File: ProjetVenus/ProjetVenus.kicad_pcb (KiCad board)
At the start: 2 copper layers, 41 parts, among them J1 Conn_01x02_Pin, J2 Conn_01x04_Pin, J4 Conn_01x02_Pin, J5 Conn_01x05_Pin, U1 ATtiny412-SS, U2 ADP2108AUJZ-3.0-R7, U3 MS5607-02BA

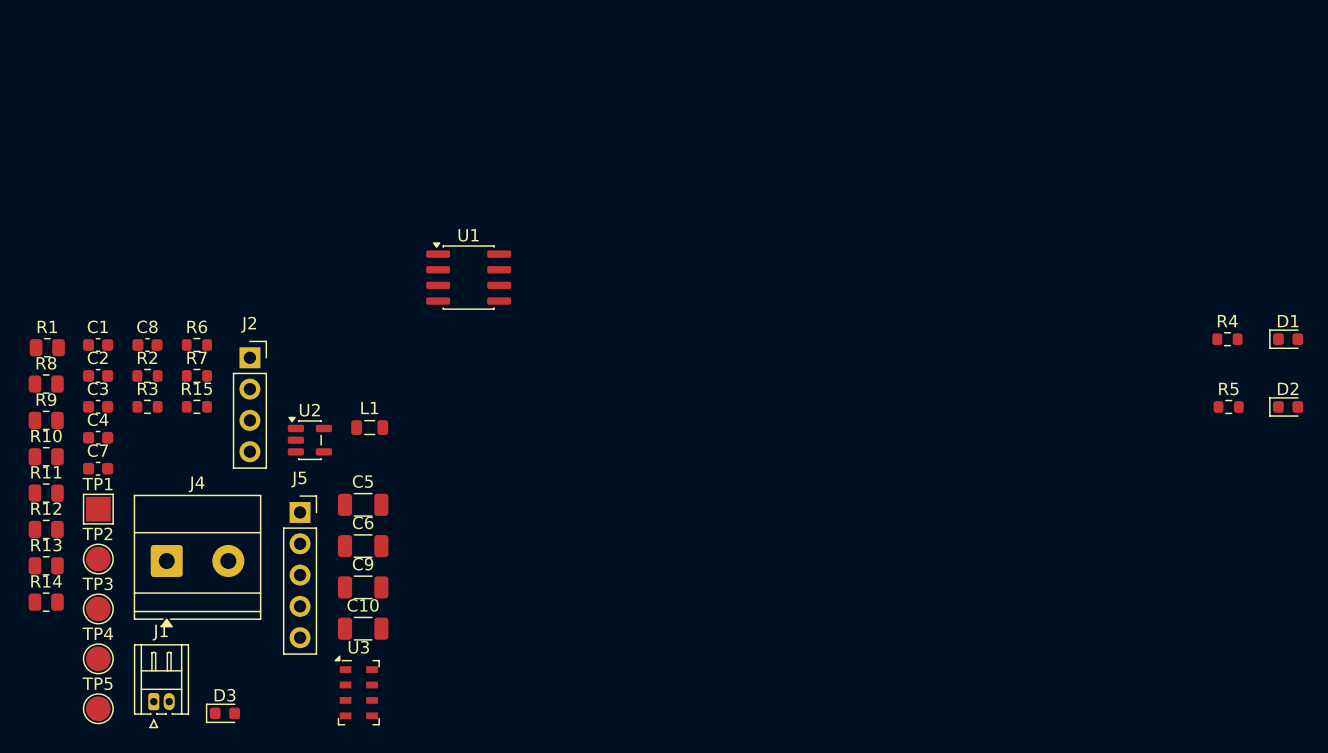
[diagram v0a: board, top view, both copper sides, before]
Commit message: V1.0
La chip U3 a du cosmétiques qui va disparaitre a moins qu'on change le footprint, mais on s'en fou un peu
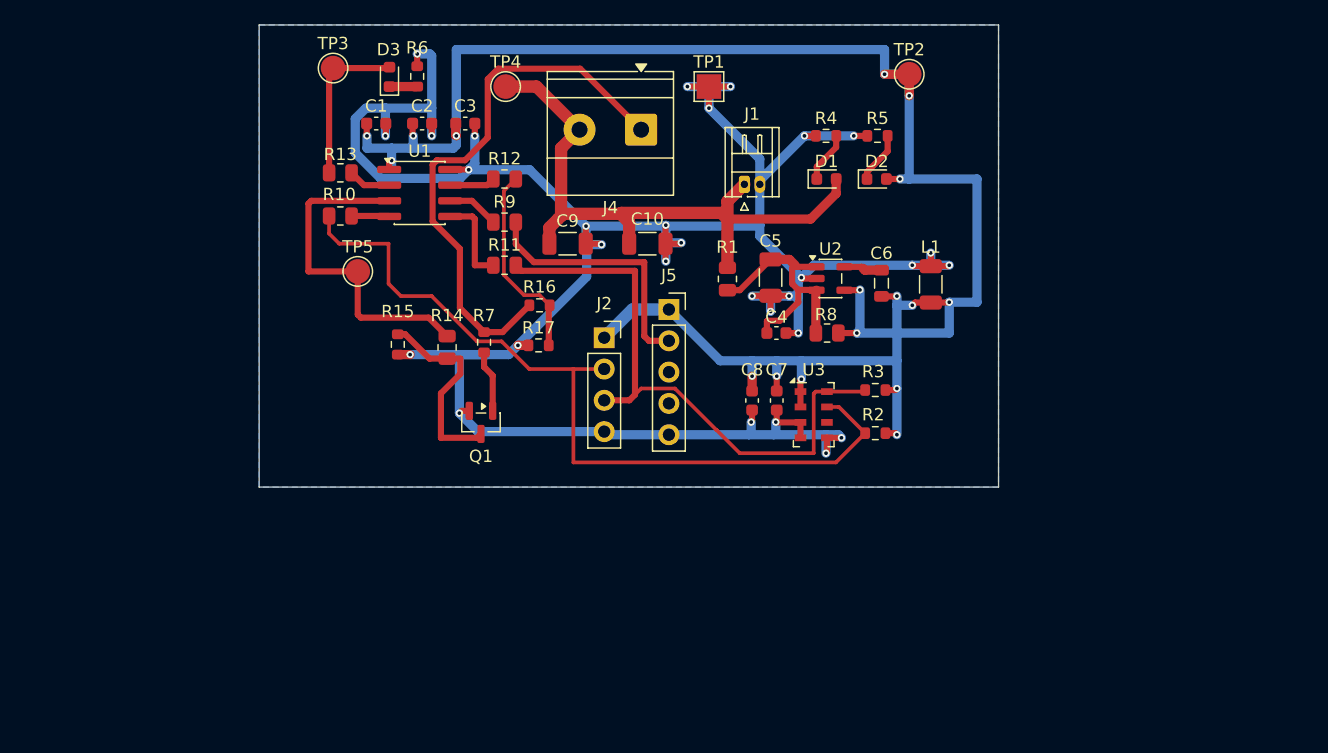
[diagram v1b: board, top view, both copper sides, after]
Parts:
- added Q1: Q_NMOS_GSD, Package_TO_SOT_SMD:SOT-23, F.Cu at (208.0, 122.2)
- added R16: 100k, Resistor_SMD:R_0603_1608Metric, F.Cu at (212.8, 112.8)
- added R17: 100k, Resistor_SMD:R_0603_1608Metric, F.Cu at (212.7, 116.0)
- R14: value TBD -> 220
- moved TP2 76.7 mm to (242.8, 94.0)
- moved J1 63.7 mm to (229.4, 102.9)
- moved R8 63.5 mm to (236.1, 115.0)
- moved TP1 60.3 mm to (226.5, 95.0)
- moved R2 59.2 mm to (240.0, 123.1)
- moved R3 59.1 mm to (240.0, 119.6)
- moved TP4 57.0 mm to (210.0, 95.0)
- moved C4 55.7 mm to (232.0, 115.0)
- moved R1 55.5 mm to (228.0, 110.6), turned to -90 degrees
- moved C7 55.3 mm to (232.0, 120.5), turned to -90 degrees
- moved D3 53.3 mm to (200.6, 94.2), turned to 90 degrees
- moved J4 52.0 mm to (221.0, 98.5), turned to 180 degrees
- moved C6 50.7 mm to (244.5, 111.0), turned to 90 degrees
- moved C8 49.3 mm to (230.0, 120.5), turned to -90 degrees
- moved TP3 47.8 mm to (196.0, 93.5)
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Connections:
- R12 pad 2: unconnected-(R12-Pad2) -> /EMATCH_DET
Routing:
- net GND: track 0.00 -> 222.7 mm, vias 0 -> 30
- net +3V0: track 0.00 -> 164.0 mm, vias 0 -> 17
- net /SDA: track 0.00 -> 66.4 mm
- net +BATT: track 0.00 -> 52.4 mm
- net /SCL: track 0.00 -> 49.1 mm
- net Net-(J4-Pin_1): track 0.00 -> 44.9 mm
- net /EMATCH: track 0.00 -> 27.6 mm
- net Net-(U2-EN): track 0.00 -> 21.1 mm
- net /UPDI: track 0.00 -> 21.0 mm
- net Net-(Q1-G): track 0.00 -> 16.7 mm
- net /EMATCH_DET: track 0.00 -> 16.2 mm
- net /LED: track 0.00 -> 13.2 mm
- net Net-(U1-PA2): track 0.00 -> 7.34 mm
- net Net-(Q1-D): track 0.00 -> 5.03 mm
- net Net-(U1-~{RESET}/PA0): track 0.00 -> 4.22 mm
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- added copper zone on B.Cu, net GND
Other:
- board outline added: 60 x 37.5 mm
- rule pad_to_mask_clearance: 0 -> 0.1
